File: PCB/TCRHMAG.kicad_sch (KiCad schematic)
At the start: 31 parts, among them J1 CONN_BATTERY, J2 CONN_LED, J3 CONN_THERM, J4 CONN_OLED, J5 CONN_HEATER, Q301 Si4116DY, SW101 PWR_SW, U101 L78L05_SOT89, U102 CH32V003FxPx

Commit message: Firmware Testing
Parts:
- added J6: CONN_PROG, TCRHMAG:Program_Conn, symbol Connector:Conn_01x04_Pin
- added R107, R108: 4K7, Resistor_SMD:R_0603_1608Metric, symbol Device:R
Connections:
- net GND: now also J4.4 (Pin_4), J6.1 (Pin_1), J6.4 (Pin_4)
- net MCU_LED_OUT: now also U102.20 (PD3)
- net MCU_SCL: now also J4.2 (Pin_2), R107.2
- net MCU_SDA: now also J4.3 (Pin_3), R108.2
- net MCU_SWIO: now also J6.3 (Pin_3)
- net PBUS_5V: now also J4.1 (Pin_1), J6.2 (Pin_2), R107.1, R108.1
- net MCU_OPAMP_OUT renamed MCU_OPAMP_ADC

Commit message: Added temperature Linear Interpolation
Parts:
- added J6: CONN_ENCODER, Connector_PinHeader_1.00mm:PinHeader_1x04_P1.00mm_Vertical, symbol Connector:Conn_01x04_Pin
- J4: footprint (none) -> Connector_PinHeader_1.00mm:PinHeader_1x04_P1.00mm_Vertical
- renumbered J6 to J7
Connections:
- net GND: now also J6.1 (Pin_1)
- net MCU_SCL: now also J4.3 (Pin_3), R108.2; no longer J4.2 (Pin_2), R107.2
- net MCU_SDA: now also J4.2 (Pin_2), R107.2; no longer J4.3 (Pin_3), R108.2
- net MCU_ENC_SW: now reaches U102.13 (PC3)
- net MCU_ENC_SW: now also J6.4 (Pin_4)
- net MCU_ENC_B: now reaches U102.14 (PC4)
- net MCU_ENC_B: now also J6.3 (Pin_3)
- net MCU_ENC_A: now reaches U102.15 (PC5)
- net MCU_ENC_A: now also J6.2 (Pin_2)
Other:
- moved on the sheet: C104, J7

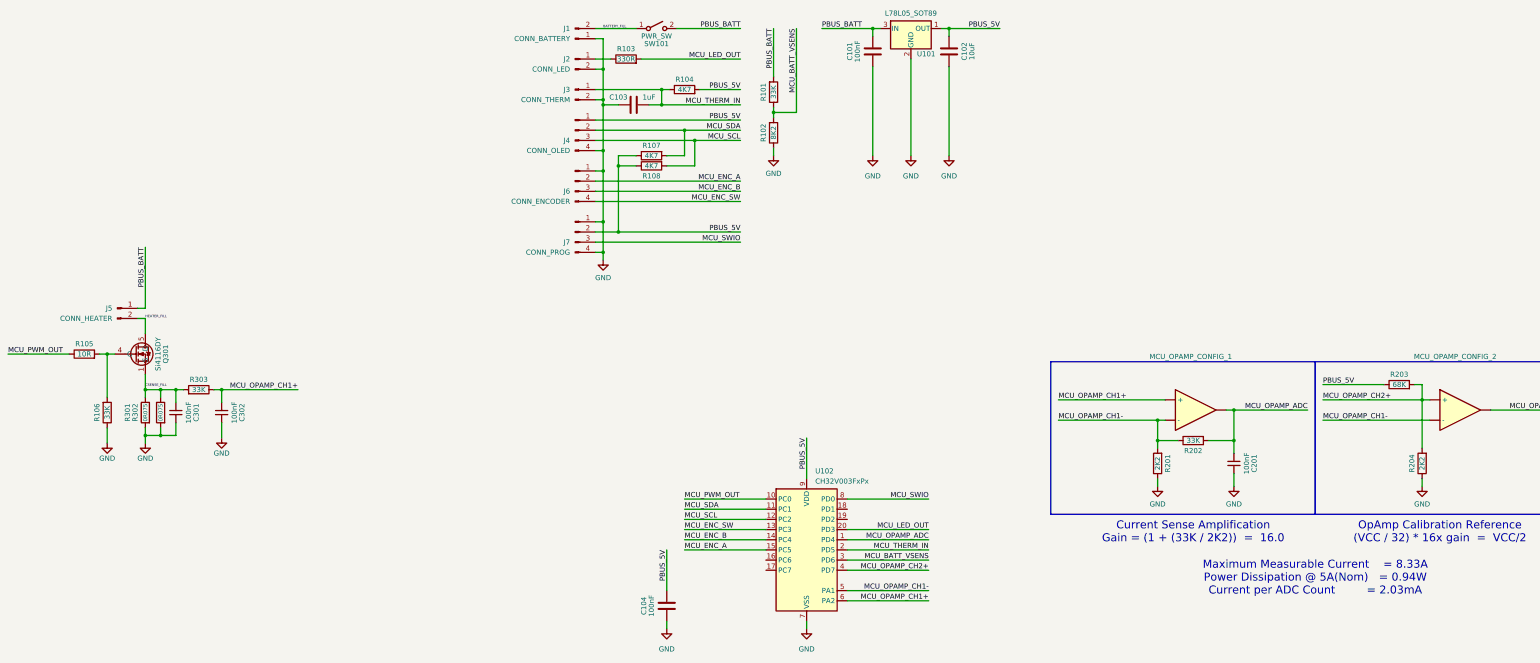
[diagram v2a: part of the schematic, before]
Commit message: PID Heater control tested and tuned
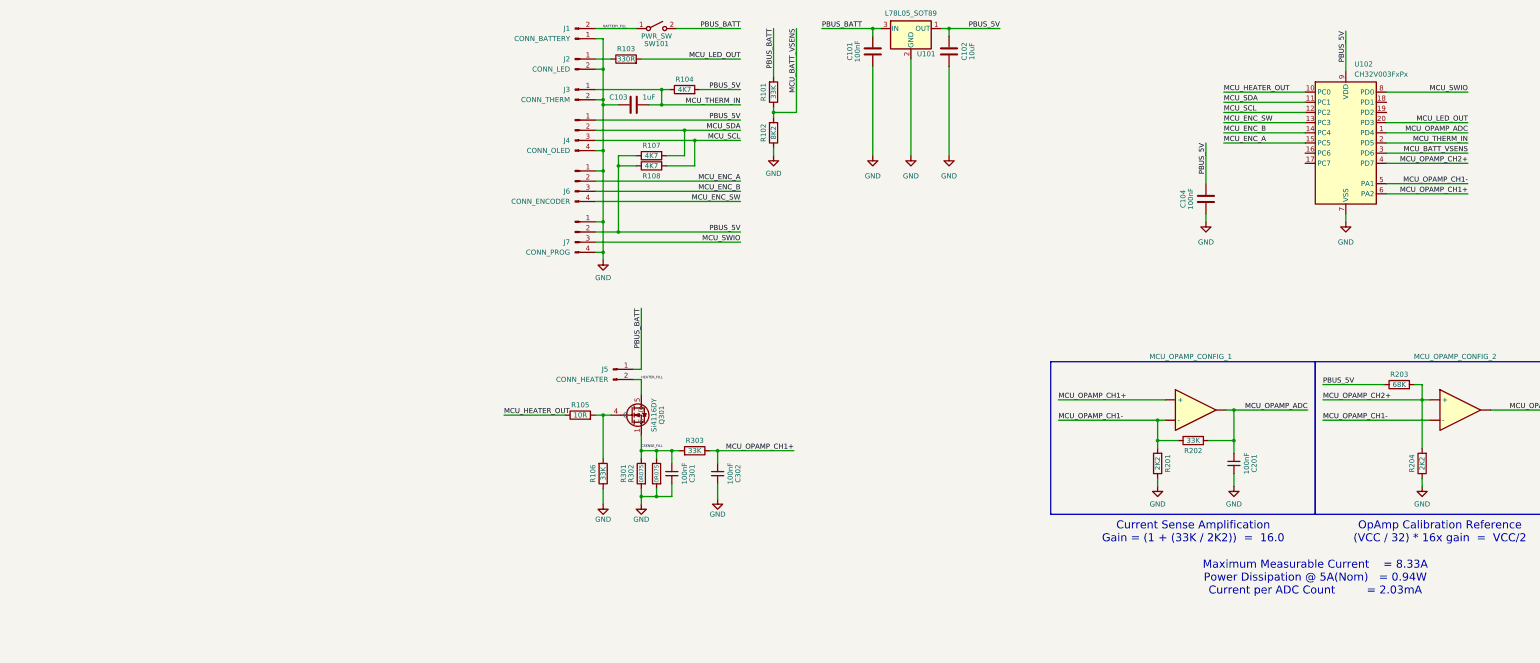
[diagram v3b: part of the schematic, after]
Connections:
- net MCU_PWM_OUT renamed MCU_HEATER_OUT
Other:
- moved on the sheet: C104, C301, C302, J5, Q301, R105, R106, R301, R302, R303, U102

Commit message: Final PCB
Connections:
- no-connect marks 0 -> 4
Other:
- moved on the sheet: C104, C301, C302, J5, Q301, R105, R106, R301, R302, R303, U102

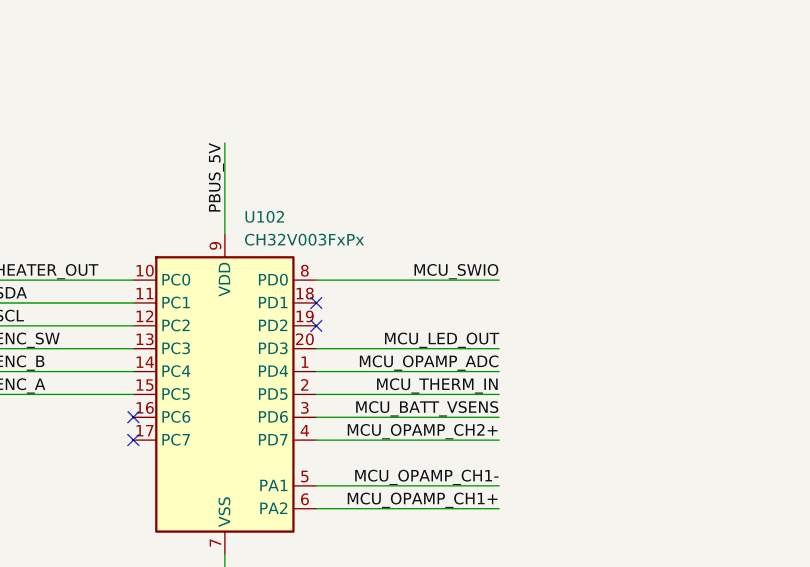
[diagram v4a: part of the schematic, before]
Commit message: Fixed SWIO Bug. MkII HW
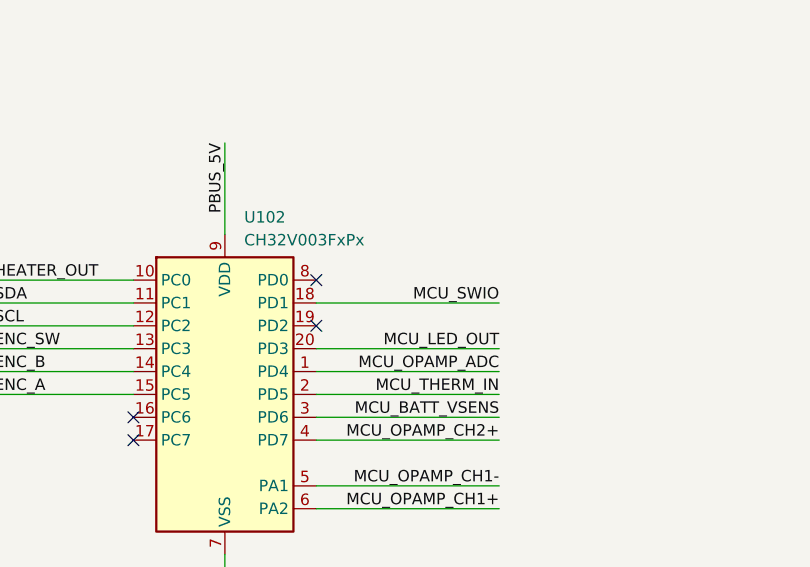
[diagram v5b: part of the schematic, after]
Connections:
- net MCU_SWIO: now also U102.18 (PD1); no longer U102.8 (PD0)
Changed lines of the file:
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@@
 	(title_block
 		(title "TCRHMAG")
-		(date "2026-03-10")
-		(rev "MkI")
+		(date "2026-03-19")
+		(rev "MkII")
 		(company "ADBeta")
 	)
@@
 	)
 	(no_connect
-		(at 90.805 130.175)
+		(at 90.805 127.635)
 	)
 	(no_connect
@@
 	(wire
 		(pts
-			(xy 90.805 127.635) (xy 111.125 127.635)
+			(xy 90.805 130.175) (xy 111.125 130.175)
 		)
 		(stroke
@@
 	)
 	(label "MCU_SWIO"
-		(at 111.125 127.635 180)
-		(effects
-			(font
+		(at 111.125 130.175 180)
+		(effects
+			(font

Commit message: MkIII PCB Finished
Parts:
- added C105: 10uF, Capacitor_SMD:C_0402_1005Metric, symbol Device:C
- added C106, C107: 10nF, Capacitor_SMD:C_0402_1005Metric, symbol Device:C
- added R109, R110, R111, R112: 4K7, Resistor_SMD:R_0402_1005Metric, symbol Device:R
- C101, C102, C103, C104, C201, C301, C302: footprint Capacitor_SMD:C_0603_1608Metric -> Capacitor_SMD:C_0402_1005Metric
- J4, J6: footprint Connector_PinHeader_1.00mm:PinHeader_1x04_P1.00mm_Vertical -> Connector_PinSocket_2.00mm:PinSocket_1x04_P2.00mm_Vertical
- MCU_OPAMP_CONFIG_1, MCU_OPAMP_CONFIG_2: value ~ -> (none)
- R101, R102, R103, R104, R105, R106, R107, R108, R201, R202, R203, R204, R303: footprint Resistor_SMD:R_0603_1608Metric -> Resistor_SMD:R_0402_1005Metric
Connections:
- net GND: now also C105.2, C106.1, C107.1
- net MCU_BATT_VSENS: now also C105.1
- net MCU_ENC_A: now also C107.2, R110.2; no longer J6.2 (Pin_2)
- net MCU_ENC_B: now also C106.2, R111.2; no longer J6.3 (Pin_3)
- net MCU_SCL: now also J4.2 (Pin_2), R107.2; no longer J4.3 (Pin_3), R108.2
- net MCU_SDA: now also J4.3 (Pin_3), R108.2; no longer J4.2 (Pin_2), R107.2
- net PBUS_5V: now also R109.2, R112.2
- net BATTERY_FILL: no longer names the net of J1.2 (Pin_2), SW101.1 (A)
- net HEATER_FILL: no longer names the net of J5.2 (Pin_2), Q301.5 (D), Q301.6 (D), Q301.7 (D), Q301.8 (D)
- new net: J6.3 (Pin_3), R111.1, R112.1
- new net: J6.2 (Pin_2), R109.1, R110.1
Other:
- moved on the sheet: C101, C102, C104, C301, C302, J5, Q301, R101, R102, R105, R106, R301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
